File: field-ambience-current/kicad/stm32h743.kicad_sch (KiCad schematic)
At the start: 35 parts, among them J10 3.5mm TRS MIDI-Out (Type A, P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, J4 SWD 1.27mm (SWCLK/GND/SWDIO), U1 STM32H743VIT6 (480MHz M7, LQF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, Y1 8MHz ABLS-8.000MHZ-B4-T (CL=1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

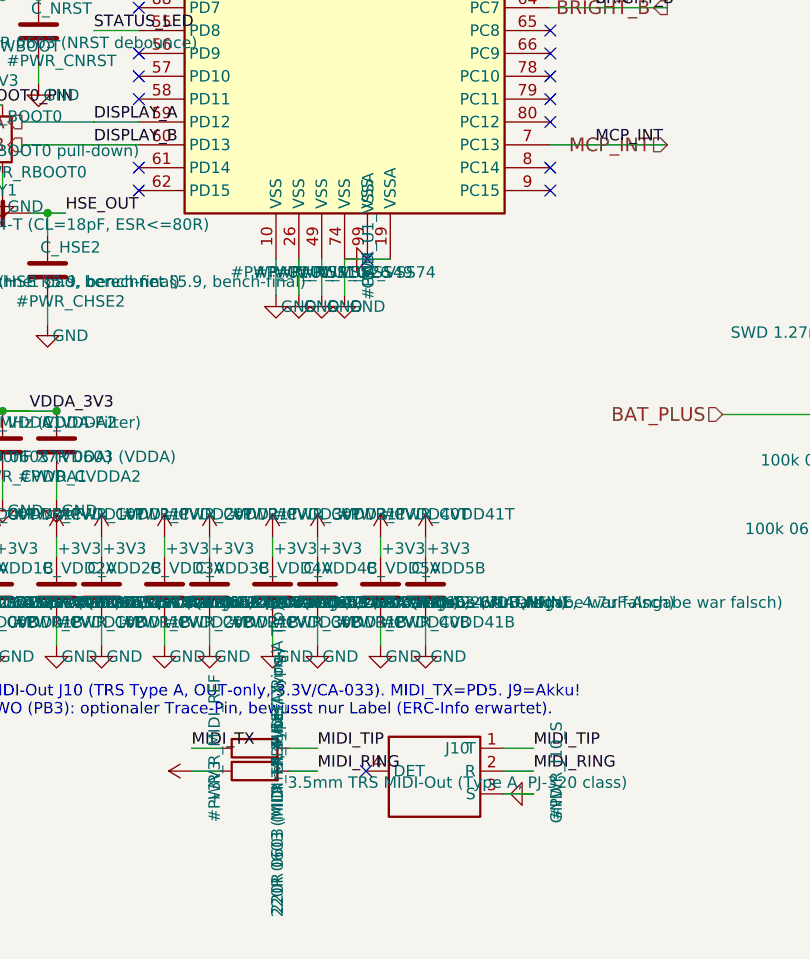
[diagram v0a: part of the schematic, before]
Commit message: fix(pcb): datasheet verification of all remaining parts — encoder + jack pad maps were dead/wrong (r18.82) (#94)
User asked to verify all other components against datasheets. Every
remaining IC and every symbol-pin<->footprint-pad pairing was checked
against the official documents (Microchip DS20001952 + DS20001984, NXP
PCA9685 Rev 4, ST USBLC6-2 + DS12110 Fig 5, Abracon via LCSC, SHOU HAN
PJ-320D, HX B3F-4055, KiCad footprint sources).

Critical pad-mapping bugs (KiCad matches pin number to pad name as a
STRING):

1. All 4 rotary encoders were completely unconnected: the official KiCad
   footprint RotaryEncoder_Alps_EC11E-Switch_Vertical_H20mm uses NAMED
   pads A/B/C/S1/S2, the custom symbol used numeric pins 1-5 - not a
   single encoder pin would have joined a pad in the netlist. Symbol pin
   numbers renamed to the pad names (footprint geometry verified from
   the KiCad GitLab source: A(0,0), C(0,2.5) = middle common, B(0,5) =
   ALPS A-C-B terminal order).

2. PJ-320D jacks (J8 line-out, J10 MIDI): pad map was wrong. The SHOU HAN
   drawing (PCB layout + schematic) assigns pad 1=A=sleeve, 2=D=ring,
   3=C=tip-switch(detect), 4=B=tip. The symbol mapped T=1/R=2/S=3/DET=4,
   which put LEFT AUDIO on the grounded sleeve barrel, GND on the detect
   contact and JACK_DETECT on the tip. Corrected to T=4/R=2/S=1/DET=3.
   Vendored footprint geometry matches the drawing exactly (3.0/4.0mm
   pad pitch, 1.0mm locators at 7.0mm) - closes TODO B0b.

3. Consequence of the true detect topology (detect rests on the TIP when
   unplugged, i.e. on the DAC L output at +-3Vpk): added R_DET_J8 10k
   (limits MCP input-clamp current to <300uA - unprotected it would have
   clamped negative half-waves through 22R at >100mA, distorting the
   speaker feed) and C_DET_J8 1uF (filters audio AC off GPA6, fc ~16Hz).
   Levels: unplugged ~0.3V LOW, plugged 3.3V HIGH.

Datasheet-required gaps:

4. MCP73831 was missing the 4.7uF VDD input capacitor from the DS typical
   application - the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
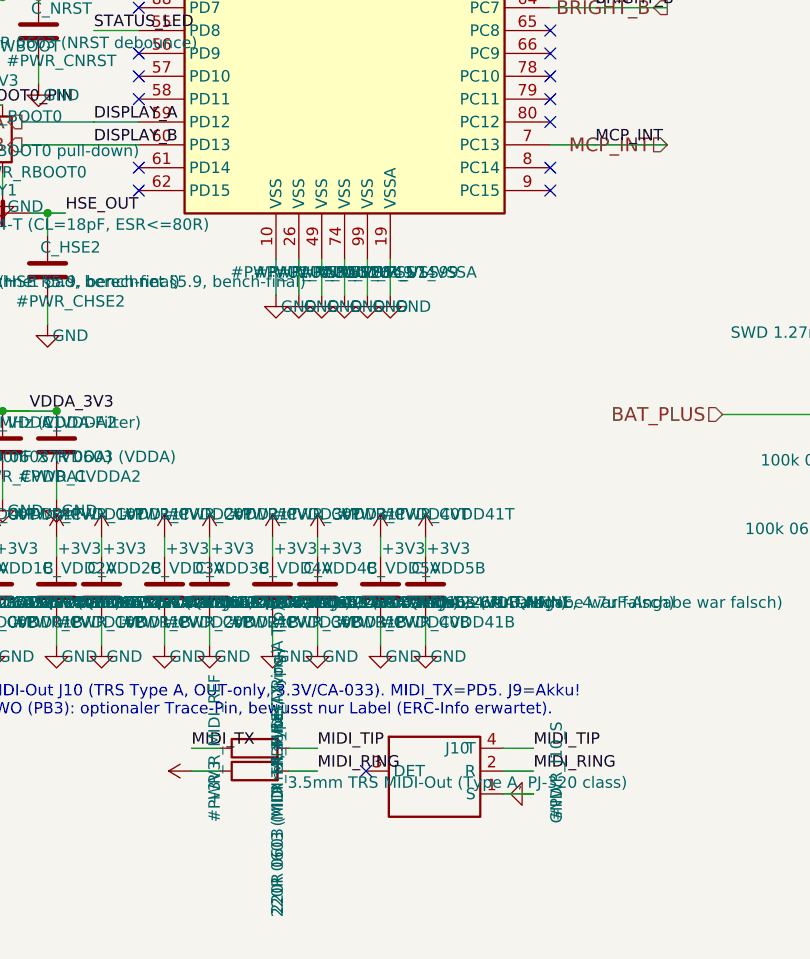
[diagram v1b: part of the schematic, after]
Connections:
- net GND: now also J10.1 (S), U1.99 (VSS); no longer J10.3 (S)
- net MIDI_TIP: now also J10.4 (T); no longer J10.1 (T)
- no-connect marks 45 -> 44
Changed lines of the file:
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@@
       (project "field_ambience"
         (path "/e3bc855f-ca21-4bea-a5ff-d24a556f7f9e" (reference "#PWR_U1_VSS74") (unit 1)))))
+  (symbol (lib_id "Power:GND") (at 142.54 205.12 0) (unit 1)
+    (in_bom yes) (on_board yes) (dnp no)
+      (property "Reference" "#PWR_U1_VSS99" (at 145.07999999999998 202.58 0)
+        (effects (font (size 1.27 1.27))))
+      (property "Value" "GND" (at 145.07999999999998 206.39000000000001 0)
+        (effects (font (size 1.27 1.27))))
+      (property "Footprint" "" (at 142.54 205.12 0)
+        (effects (font (size 1.27 1.27)) hide))
+      (property "Datasheet" "~" (at 142.54 205.12 0)
+        (effects (font (size 1.27 1.27)) hide))
+    (instances
+      (project "field_ambience"
+        (path "/e3bc855f-ca21-4bea-a5ff-d24a556f7f9e" (reference "#PWR_U1_VSS99") (unit 1)))))
   (symbol (lib_id "Power:+3V3") (at 134.92 57.42 0) (unit 1)
     (in_bom yes) (on_board yes) (dnp no)
@@
       (project "field_ambience"
         (path "/e3bc855f-ca21-4bea-a5ff-d24a556f7f9e" (reference "#PWR_U1_VDD6") (unit 1)))))
-  (symbol (lib_id "Power:GND") (at 140.08 201.12 90) (unit 1)
-    (in_bom yes) (on_board yes) (dnp no)
-      (property "Reference" "#PWR_U1_VSSA" (at 142.62 198.58 0)
-        (effects (font (size 1.27 1.27))))
-      (property "Value" "GND" (at 142.62 202.39000000000001 0)
-        (effects (font (size 1.27 1.27))))
-      (property "Footprint" "" (at 140.08 201.12 0)
-        (effects (font (size 1.27 1.27)) hide))
-      (property "Datasheet" "~" (at 140.08 201.12 0)
+  (symbol (lib_id "Power:GND") (at 145.08 205.12 0) (unit 1)
+    (in_bom yes) (on_board yes) (dnp no)
+      (property "Reference" "#PWR_U1_VSSA" (at 147.62 202.58 0)
+        (effects (font (size 1.27 1.27))))
+      (property "Value" "GND" (at 147.62 206.39000000000001 0)
+        (effects (font (size 1.27 1.27))))
+      (property "Footprint" "" (at 145.08 205.12 0)
+        (effects (font (size 1.27 1.27)) hide))
+      (property "Datasheet" "~" (at 145.08 205.12 0)
         (effects (font (size 1.27 1.27)) hide))
     (instances
@@
     (stroke (width 0) (type default))
 )
+  (wire (pts (xy 142.54 201.12) (xy 142.54 205.12))
+    (stroke (width 0) (type default))
+)
   (wire (pts (xy 134.92 61.42) (xy 134.92 57.42))
     (stroke (width 0) (type default))
@@
     (stroke (width 0) (type default))
 )
-  (wire (pts (xy 145.08 201.12) (xy 140.08 201.12))
+  (wire (pts (xy 145.08 201.12) (xy 145.08 205.12))
     (stroke (width 0) (type default))
 )
@@
   (no_connect (at 162.86 135.08)
 )
-  (no_connect (at 142.54 201.12)
-)
   (text "MIDI-Out J10 (TRS Type A, OUT-only, 3.3V/CA-033). MIDI_TX=PD5. J9=Akku!" (at 100 250 0)

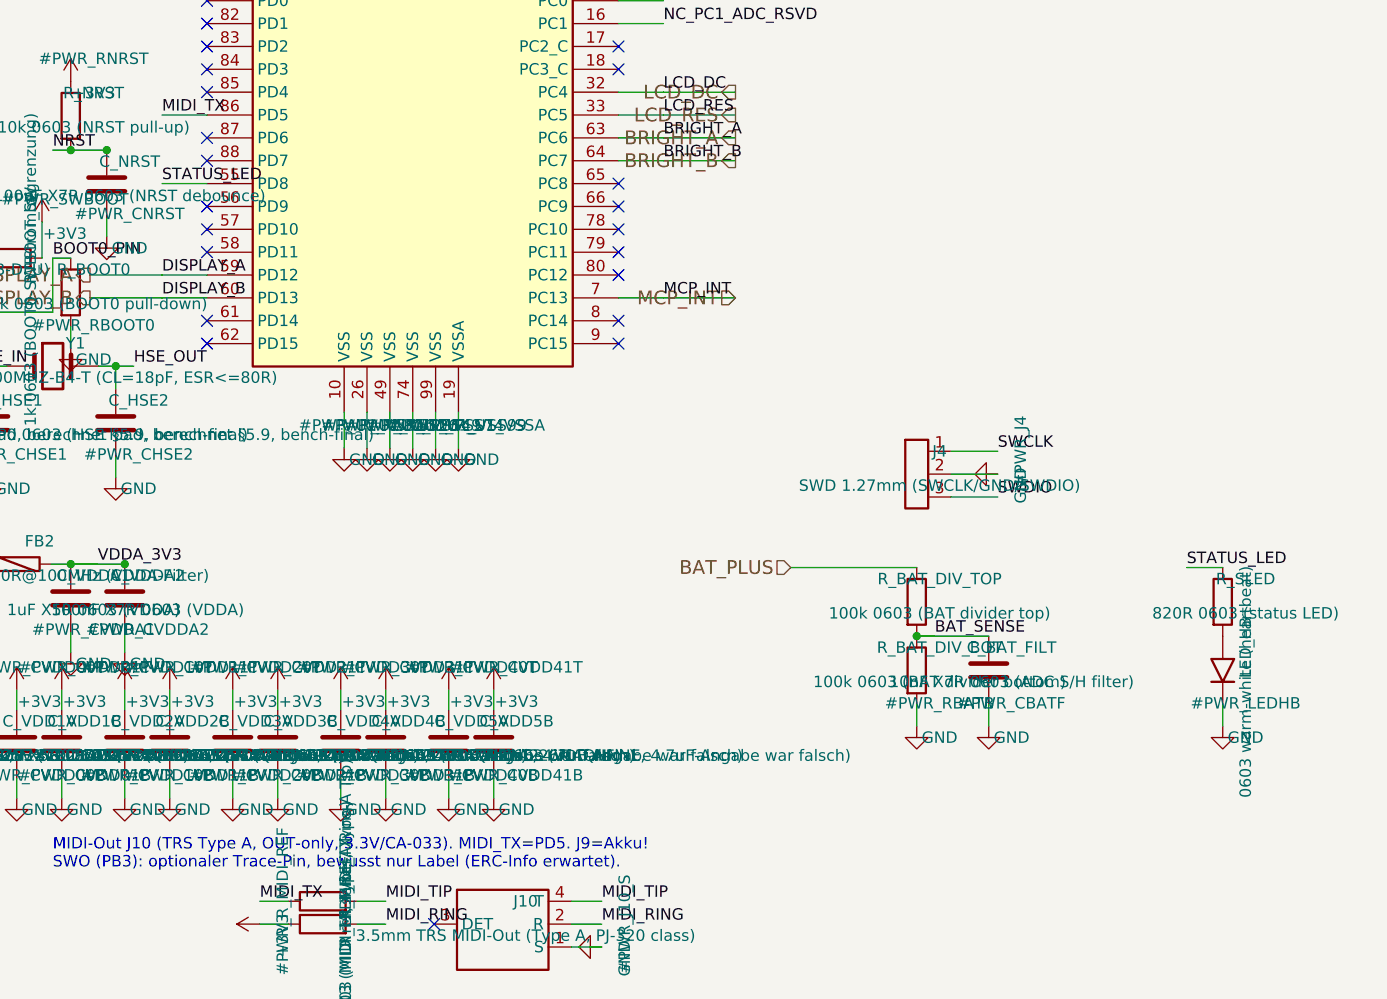
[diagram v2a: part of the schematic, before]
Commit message: feat(pcb+firmware): keep only cell + modifier LEDs — remove VU meter (U10) + heartbeat LED; fresh audio renders (r18.87)
User directive: only the LEDs above the cells and above the modifier
buttons stay.

Schematic (generator, regenerated + geometric ERC 0 errors):
- mcp_sheet: U10 PCA9685 #2 (0x41) + LED_VU1-8 + R_VU1-8 + R_OE2 +
  C_PCA2_VDD/_HF removed; I2C bus back to U2 (0x20) + U6 (0x40) only
- stm32h743_sheet: LED_HB + R_SLED (STATUS_LED) removed, PD8 parked as
  NC reserve
- LED_CHRG deliberately kept: with ADR-0016 the device charges while
  switched OFF (no firmware running) — the hardware-driven MCP73831
  STAT LED is the only charge feedback

BOM/docs: jlc_bom.csv 57 parts / 188 placements (-22), SMD BOM/board
$24.50 -> ~$21.30, 5-run ~$89 (Economic) / ~$99 (Standard) per device;
BOM_MASTER, PCB_BOM, COST_ESTIMATE, PCB_HANDOFF, onboarding,
bom_overview.html updated; ADR-0020 marked SUPERSEDED.

Firmware: vu.{h,c} + test_vu.c deleted, pca2_*/PCA2_I2C_ADDR API and
main-loop VU block removed, engine_render_peak() tap removed. Host
suite 24 suites / 0 failures; h743 cross-build green (152.9 KB flash).

Audio: both demo pieces re-rendered from the current engine into
demos/audio/ — field_ambience_master_tape.flac (8:20, peak -6.7 dBFS)
and field_ambience_performance.flac (5:00, peak -4.7 dBFS), flac -t
verified; README pointer updated.

Co-Authored-By: Claude Fable 5 <noreply@anthropic.com>
Claude-Session: https://claude.ai/code/session_019pKguH6aG4iazMCWJnpmMn
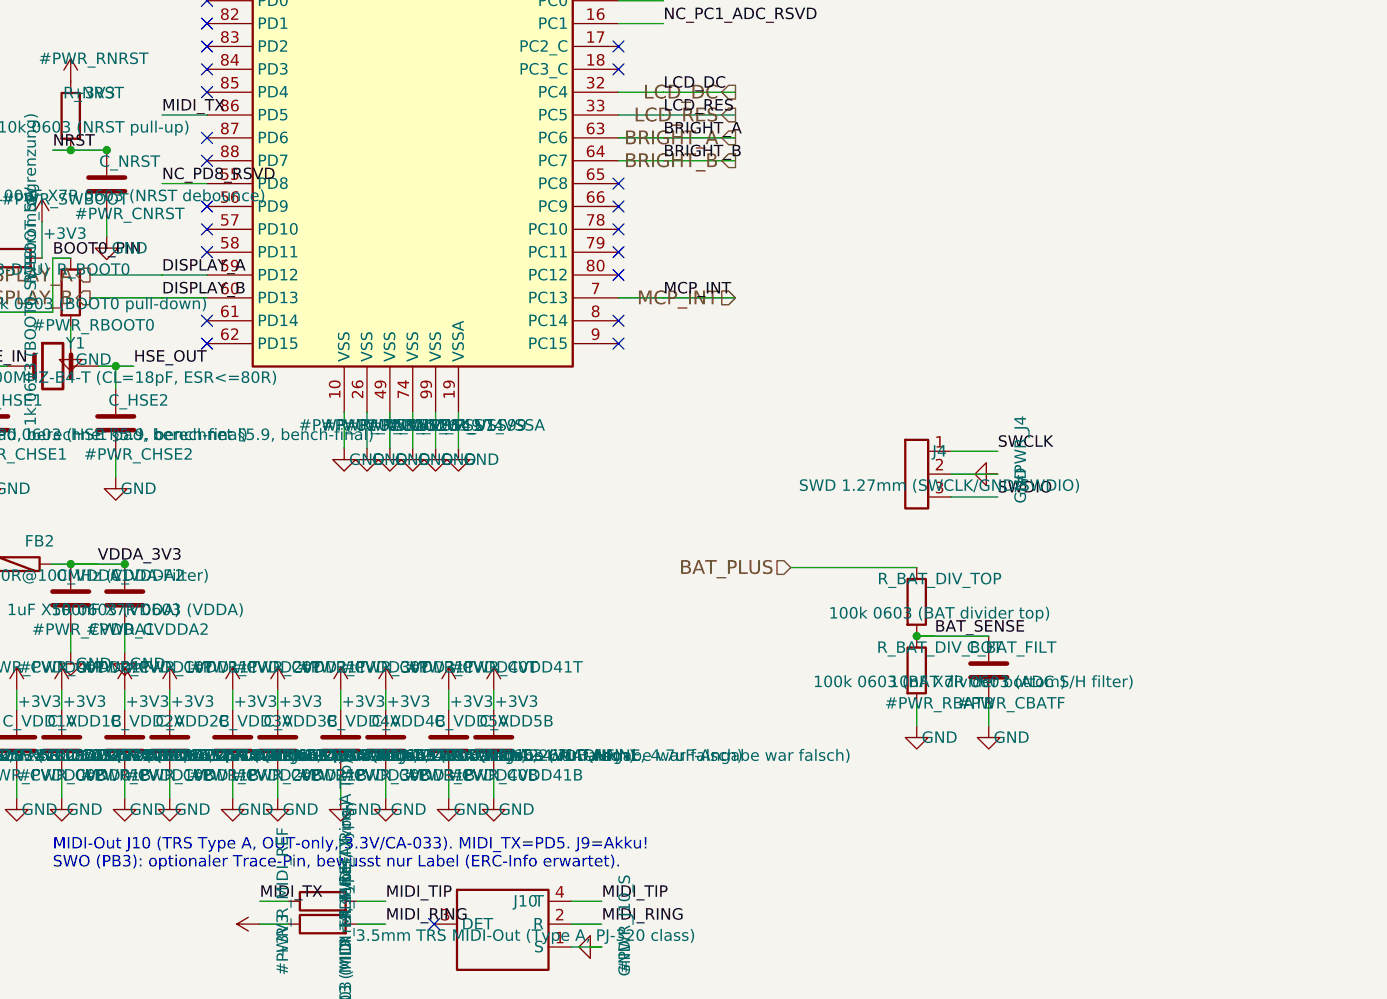
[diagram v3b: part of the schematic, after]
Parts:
- removed LED_HB: 0603 warm-white (heartbeat), LED_SMD:LED_0603_1608Metric, symbol Device:LED
- removed R_SLED: 820R 0603 (status LED), Resistor_SMD:R_0603_1608Metric, symbol Device:R
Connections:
- net STATUS_LED renamed NC_PD8_RSVD
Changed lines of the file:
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@@
       (project "field_ambience"
         (path "/e3bc855f-ca21-4bea-a5ff-d24a556f7f9e" (reference "#PWR_CBATF") (unit 1)))))
-  (symbol (lib_id "Device:R") (at 230.0 222.19 0) (unit 1)
-    (in_bom yes) (on_board yes) (dnp no)
-      (property "Reference" "R_SLED" (at 232.54 219.65 0)
-        (effects (font (size 1.27 1.27))))
-      (property "Value" "820R 0603 (status LED)" (at 232.54 223.46 0)
-        (effects (font (size 1.27 1.27))))
-      (property "Footprint" "Resistor_SMD:R_0603_1608Metric" (at 230.0 222.19 0)
-        (effects (font (size 1.27 1.27)) hide))
-      (property "Datasheet" "~" (at 230.0 222.19 0)
-        (effects (font (size 1.27 1.27)) hide))
-      (property "MPN" "0603WAF8200T5E" (at 232.54 226.0 0)
-        (effects (font (size 1.27 1.27)) hide))
-      (property "LCSC" "C23253" (at 232.54 227.27 0)
-        (effects (font (size 1.27 1.27)) hide))
-    (instances
-      (project "field_ambience"
-        (path "/e3bc855f-ca21-4bea-a5ff-d24a556f7f9e" (reference "R_SLED") (unit 1)))))
-  (symbol (lib_id "Device:LED") (at 230.0 229.81 90) (unit 1)
-    (in_bom yes) (on_board yes) (dnp no)
-      (property "Reference" "LED_HB" (at 232.54 227.27 0)
-        (effects (font (size 1.27 1.27))))
-      (property "Value" "0603 warm-white (heartbeat)" (at 232.54 231.08 0)
-        (effects (font (size 1.27 1.27))))
-      (property "Footprint" "LED_SMD:LED_0603_1608Metric" (at 230.0 229.81 0)
-        (effects (font (size 1.27 1.27)) hide))
-      (property "Datasheet" "~" (at 230.0 229.81 0)
-        (effects (font (size 1.27 1.27)) hide))
-      (property "MPN" "XL-1608UWC-04" (at 232.54 233.62 0)
-        (effects (font (size 1.27 1.27)) hide))
-      (property "LCSC" "C965808" (at 232.54 234.89000000000001 0)
-        (effects (font (size 1.27 1.27)) hide))
-    (instances
-      (project "field_ambience"
-        (path "/e3bc855f-ca21-4bea-a5ff-d24a556f7f9e" (reference "LED_HB") (unit 1)))))
-  (symbol (lib_id "Power:GND") (at 230.0 236.0 0) (unit 1)
-    (in_bom yes) (on_board yes) (dnp no)
-      (property "Reference" "#PWR_LEDHB" (at 232.54 233.46 0)
-        (effects (font (size 1.27 1.27))))
-      (property "Value" "GND" (at 232.54 237.27 0)
-        (effects (font (size 1.27 1.27))))
-      (property "Footprint" "" (at 230.0 236.0 0)
-        (effects (font (size 1.27 1.27)) hide))
-      (property "Datasheet" "~" (at 230.0 236.0 0)
-        (effects (font (size 1.27 1.27)) hide))
-    (instances
-      (project "field_ambience"
-        (path "/e3bc855f-ca21-4bea-a5ff-d24a556f7f9e" (reference "#PWR_LEDHB") (unit 1)))))
   (symbol (lib_id "Connector:AudioJack3_Switch") (at 150 258 0) (unit 1)
     (in_bom yes) (on_board yes) (dnp no)
@@
     (stroke (width 0) (type default))
 )
-  (wire (pts (xy 226.0 218.38) (xy 230.0 218.38))
-    (stroke (width 0) (type default))
-)
-  (wire (pts (xy 230.0 233.62) (xy 230.0 236.0))
-    (stroke (width 0) (type default))
-)
   (wire (pts (xy 157.62 255.46) (xy 161 255.46))
     (stroke (width 0) (type default))
@@
     (effects (font (size 1.27 1.27)) (justify left bottom))
 )
-  (label "STATUS_LED" (at 112.14 175.72 0) (fields_autoplaced)
+  (label "NC_PD8_RSVD" (at 112.14 175.72 0) (fields_autoplaced)
     (effects (font (size 1.27 1.27)) (justify left bottom))
 )
@@
     (effects (font (size 1.27 1.27)) (justify left bottom))
 )
-  (label "STATUS_LED" (at 226.0 218.38 0) (fields_autoplaced)
-    (effects (font (size 1.27 1.27)) (justify left bottom))
-)
